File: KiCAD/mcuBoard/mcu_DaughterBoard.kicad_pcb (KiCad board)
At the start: 4 copper layers, 31.7 x 29 mm, 23 parts, among them SW1 NRST, SW2 BOOT0, U1 AP2112K-3.3, U2 STM32F072CBTx, U3 USBLC6-2SC6

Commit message: Fixed net names, columns and rows were switched.
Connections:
- net ROW10 renamed COL10
- net ROW11 renamed COL11
- net ROW12 renamed COL12
- net ROW13 renamed COL13
- net ROW14 renamed COL14
- net ROW15 renamed COL15
- net ROW16 renamed COL16
- net ROW17 renamed COL17
- net ROW7 renamed COL7
- net ROW8 renamed COL8
- net ROW9 renamed COL9
- CNN1 pad 1: COL1 -> ROW1
- CNN1 pad 10: ROW4 -> COL4
- CNN1 pad 11: ROW5 -> COL5
- CNN1 pad 12: ROW6 -> COL6
- CNN1 pad 2: COL2 -> ROW2
- CNN1 pad 3: COL3 -> ROW3
- CNN1 pad 4: COL4 -> ROW4
- CNN1 pad 5: COL5 -> ROW5
- CNN1 pad 6: COL6 -> ROW6
- CNN1 pad 7: ROW1 -> COL1
- CNN1 pad 8: ROW2 -> COL2
- CNN1 pad 9: ROW3 -> COL3
- U2 pad 11: ROW6 -> COL6
- U2 pad 12: ROW5 -> COL5
- U2 pad 13: ROW4 -> COL4
- U2 pad 14: ROW3 -> COL3
- U2 pad 38: COL1 -> ROW1
- U2 pad 39: COL2 -> ROW2
- U2 pad 40: COL3 -> ROW3
- U2 pad 41: COL4 -> ROW4
- U2 pad 42: COL5 -> ROW5
- U2 pad 43: COL6 -> ROW6
- U2 pad 45: ROW1 -> COL1
- U2 pad 46: ROW2 -> COL2
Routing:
- net ROW4: track 26.3 -> 16.9 mm, vias 1 -> 0
- net COL4: track 16.9 -> 26.3 mm, vias 0 -> 1
- net ROW1: track 14.6 -> 23.9 mm
- net COL1: track 23.9 -> 14.6 mm
- net ROW5: track 24.3 -> 16.2 mm, vias 1 -> 0
- net COL5: track 16.2 -> 24.3 mm, vias 0 -> 1
- net ROW3: track 26.6 -> 19.1 mm, vias 1 -> 0
- net COL3: track 19.1 -> 26.6 mm, vias 0 -> 1
- net ROW6: track 22.1 -> 15.3 mm, vias 1 -> 0
- net COL6: track 15.3 -> 22.1 mm, vias 0 -> 1
- net ROW2: track 14.6 -> 21.3 mm, vias 1 -> 0
- net COL2: track 21.3 -> 14.6 mm, vias 0 -> 1

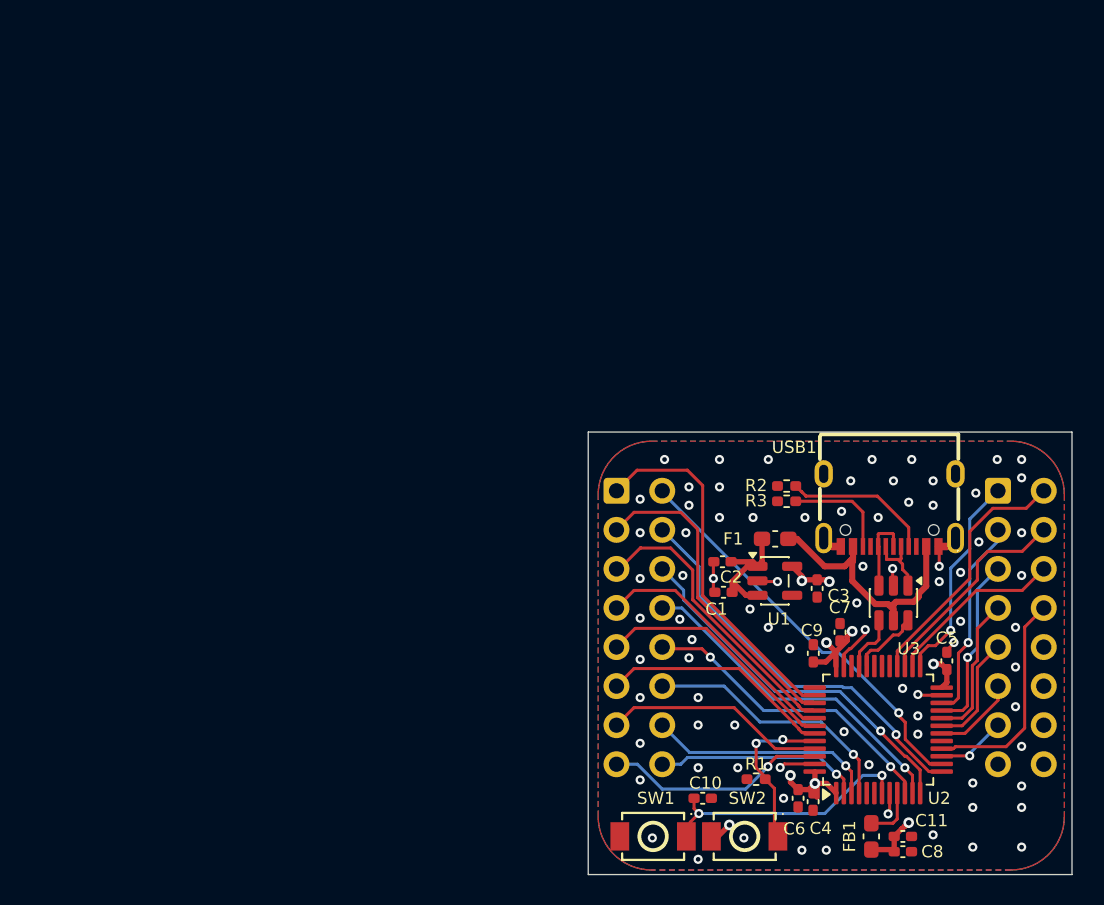
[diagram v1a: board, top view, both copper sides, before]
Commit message: MCU board has been mounted on to the keyboard PCB. Need to check if spacing is appropriate irl using calipers. Then do mounting holes using star point grounding due to use with metal chassis. ie seperate net found mounting and ground pours, which only connect at the MCU pin.
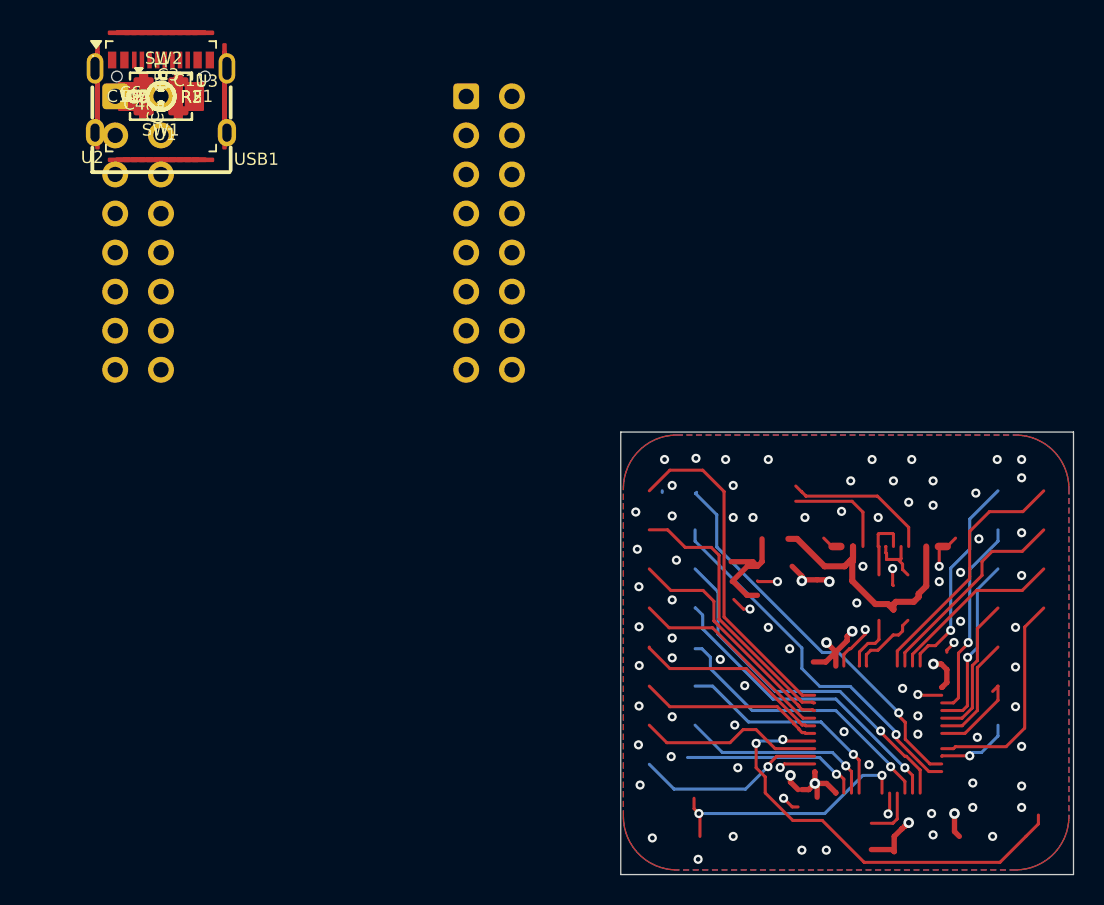
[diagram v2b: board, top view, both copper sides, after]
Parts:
- moved C8 69.4 mm to (0.00, 0.00), turned to 0 degrees
- moved C11 68.7 mm to (0.00, 0.00)
- moved FB1 67.2 mm to (0.00, 0.00), turned to 0 degrees
- moved C5 63.4 mm to (0.00, 0.00), turned to 0 degrees
- moved C4 62.9 mm to (0.00, 0.00), turned to 0 degrees
- moved U2 62.7 mm to (0.00, 0.00), turned to 0 degrees
- moved C6 62.1 mm to (0.00, 0.00), turned to 0 degrees
- moved SW2 61.8 mm to (0.00, 0.00)
- moved R1 59.4 mm to (0.00, 0.00)
- moved U3 58.4 mm to (0.00, 0.00), turned to 0 degrees
- moved SW1 58.2 mm to (0.00, 0.00)
- moved C10 58.1 mm to (0.00, 0.00), turned to 0 degrees
- moved C7 56.7 mm to (0.00, 0.00), turned to 0 degrees
- moved C9 56.2 mm to (0.00, 0.00), turned to 0 degrees
- moved USB1 54.9 mm to (0.00, 0.00), turned to 0 degrees
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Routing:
- net /BOOT0: track 11.2 -> 28.9 mm
- net ROW3: track 19.1 -> 15.5 mm
- net ROW2: track 21.3 -> 18.0 mm
- net ROW5: track 16.2 -> 13.0 mm
- net ROW6: track 15.3 -> 12.2 mm
- net ROW4: track 16.9 -> 13.8 mm
- net COL1: track 14.6 -> 12.2 mm
- net COL8: track 17.1 -> 14.9 mm
- net COL9: track 15.1 -> 12.9 mm
- net COL2: track 14.6 -> 12.5 mm
- net COL4: track 26.3 -> 24.2 mm
- net COL10: track 13.6 -> 11.7 mm
- net COL7: track 20.4 -> 18.7 mm, vias 2 -> 1
- net +3V3: track 23.5 -> 21.8 mm
- net COL6: track 22.1 -> 20.5 mm
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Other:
- board size 31.7 x 29 mm -> 29.7 x 29 mm

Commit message: Added SWD connector headers. Touched up routing on both boards.
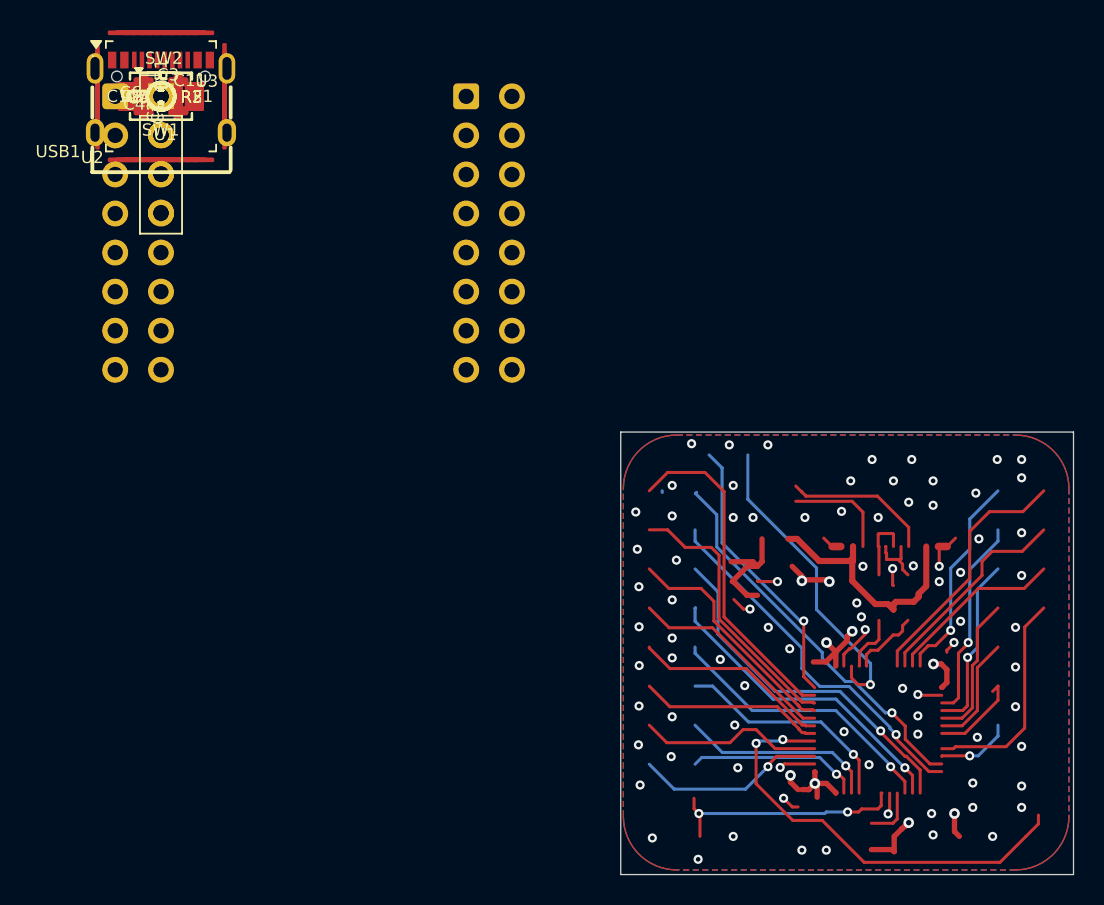
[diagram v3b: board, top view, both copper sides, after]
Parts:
- added J1: Conn_SWD, Connector_PinHeader_2.54mm:PinHeader_1x04_P2.54mm_Vertical, F.Cu at (0.00, 0.00)
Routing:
- net SWDIO: track 0.00 -> 20.6 mm, vias 0 -> 1
- net SWCLK: track 0.00 -> 18.4 mm, vias 0 -> 1
- net /NRST: track 16.9 -> 15.7 mm
- net GND: vias 83 -> 84

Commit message: Gerber files generated, small touch ups to pass DRC. Ready for purchase.
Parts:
- added G***: LOGO, test:test, B.Cu at (0.00, 0.00)
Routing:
- net GND: track 18.2 -> 20.5 mm, vias 84 -> 86
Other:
- board size 29.7 x 29 mm -> 29.8 x 29 mm
- board text added: "CG V1.0"

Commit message: Added silly logo, regenerated gerber
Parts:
- removed the G*** at (0.00, 0.00)
- added G***: LOGO, LOGO, B.Cu at (0.00, 0.00)
